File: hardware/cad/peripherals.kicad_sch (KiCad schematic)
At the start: 31 parts, among them J12 6-440054-2, J13 6-440054-2, J14 6-440129-2, J15 6-440129-2, J17 6-440054-2, J18 6-440054-2, J19 6-440129-2, J20 6-440129-2, Q1 DMN63D8LDW, SW1 FOOTSWITCH, SW2 FOOTSWITCH, U2 74LVC2G17

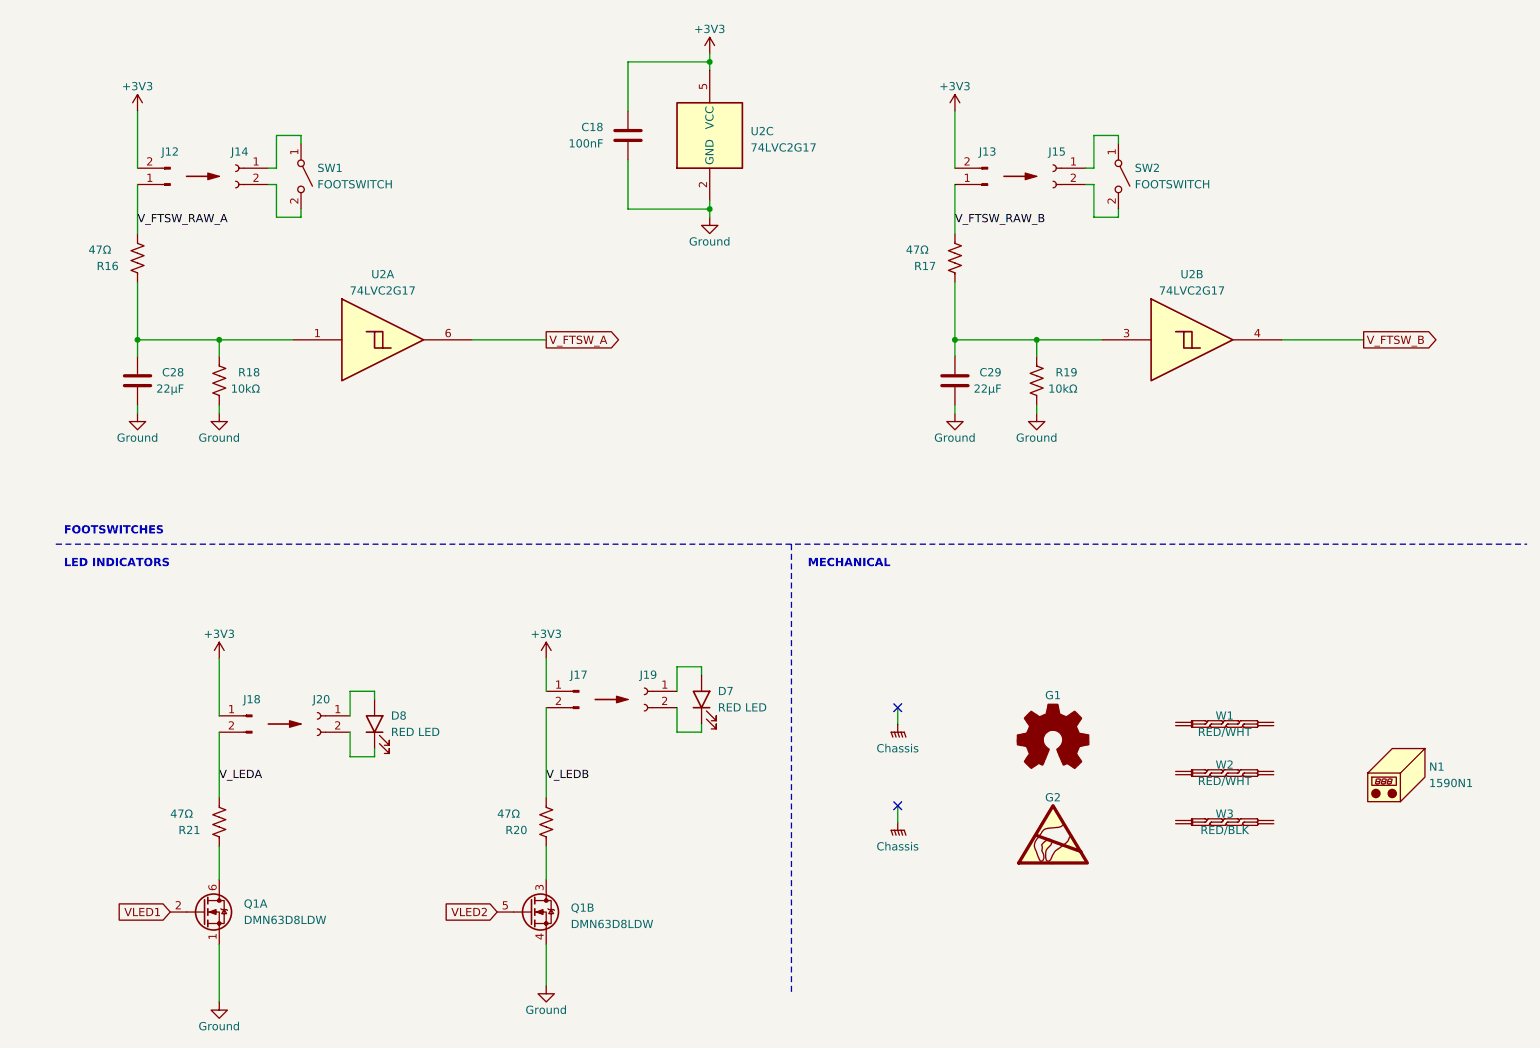
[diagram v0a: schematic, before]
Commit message: added differential inputs and started new layout
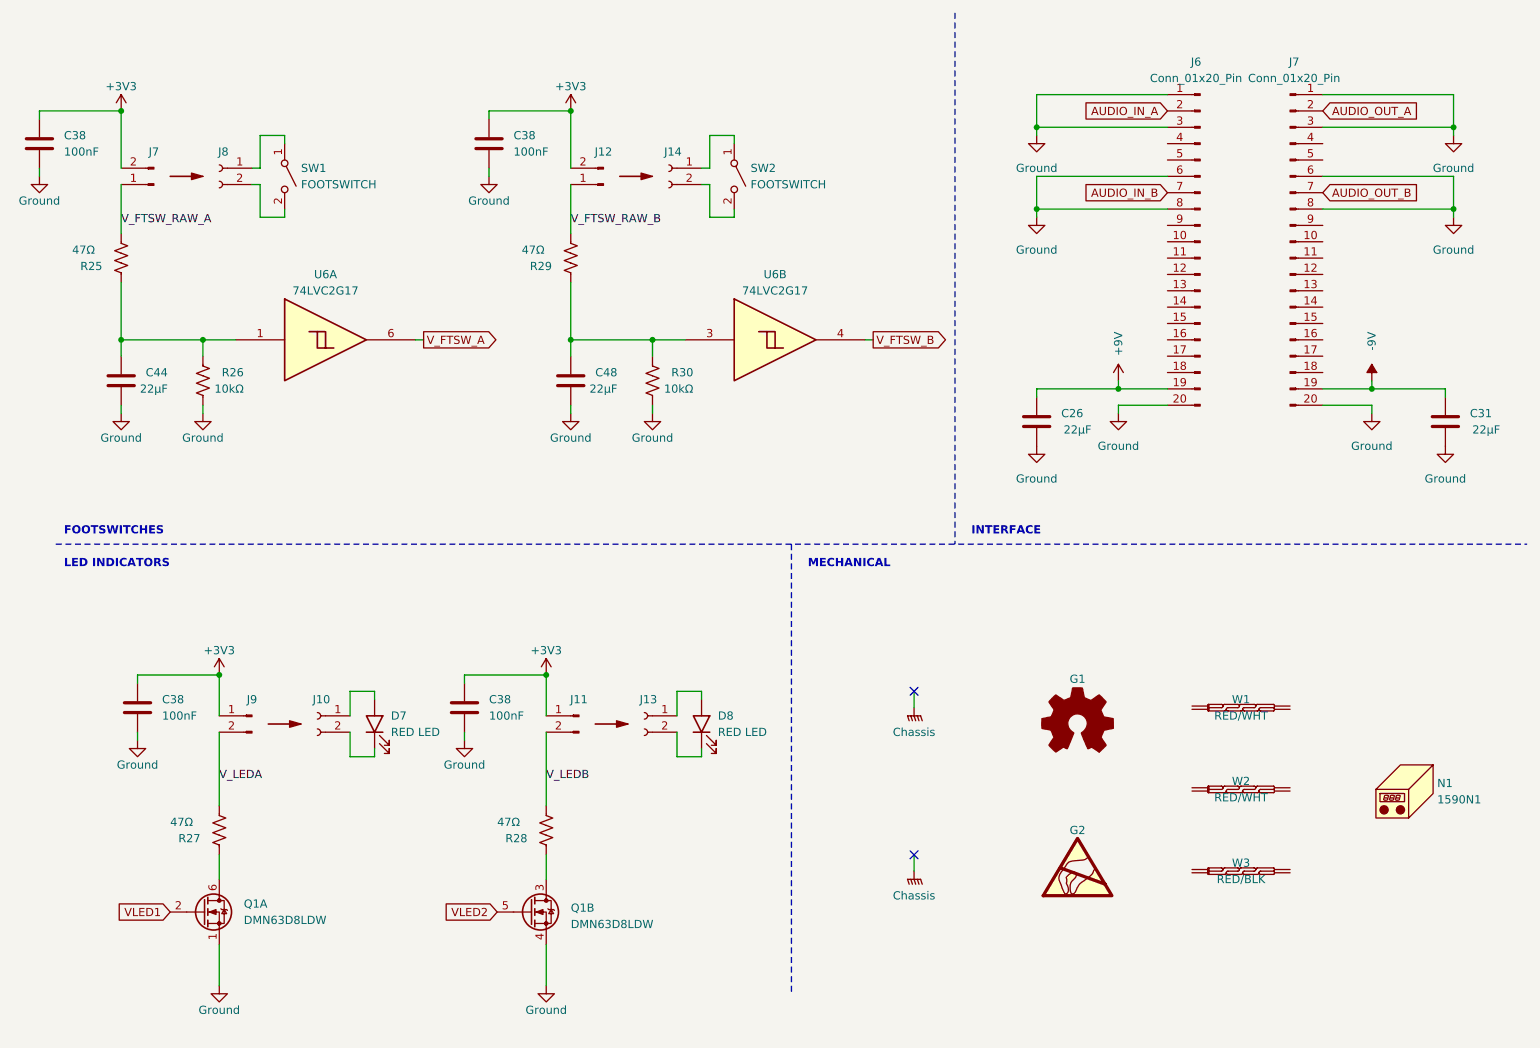
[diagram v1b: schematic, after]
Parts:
- removed C18: 100nF, Capacitor_SMD:C_0805_2012Metric, symbol Device:C
- removed unit 3 of U2
- added C26, C31: 22μF, Capacitor_SMD:C_0805_2012Metric, symbol Device:C
- added C38 (x4): 100nF, Capacitor_SMD:C_0805_2012Metric, symbol Device:C
- added J6, J7: Conn_01x20_Pin, Connector_PinSocket_2.54mm:PinSocket_1x20_P2.54mm_Vertical, symbol Connector:Conn_01x20_Pin
- renumbered C28 to C44, C29 to C48, D8 to D7, D7 to D8, J20 to J10, J17 to J11, J13 to J12, J19 to J13, J15 to J14, J12 to J7, J14 to J8, J18 to J9, R16 to R25, R18 to R26, R21 to R27, R20 to R28, R17 to R29, R19 to R30, U2 to U6
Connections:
- net +3V3: now also C38.2, C38.2, C38.2, C38.2
- net GND: now also C26.1, C31.1, C38.1, C38.1, C38.1, C38.1, J6.1 (Pin_1), J6.20 (Pin_20), J6.3 (Pin_3), J6.6 (Pin_6), J6.8 (Pin_8), J7.1 (Pin_1), J7.20 (Pin_20), J7.3 (Pin_3), J7.6 (Pin_6), J7.8 (Pin_8)
- new net +9V: C26.2, J6.19 (Pin_19)
- new net -9V: C31.2, J7.19 (Pin_19)
- new net AUDIO_IN_A: J6.2 (Pin_2)
- new net AUDIO_IN_B: J6.7 (Pin_7)
- new net AUDIO_OUT_A: J7.2 (Pin_2)
- new net AUDIO_OUT_B: J7.7 (Pin_7)
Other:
- note added: "INTERFACE"
- moved on the sheet: C44, C48, D8, G1, G2, J11, J12, J13, J14, J7, J8, N1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

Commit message: more layout updates
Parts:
- C26, C31: value 22μF -> 22u
- C38: value 100nF -> 100n
- C41: renamed from C44; value 22μF -> 22u
- C45: renamed from C48; value 22μF -> 22u
- R25, R27, R28, R29: value 47Ω -> 47R
- R26, R30: value 10kΩ -> 10k
- renumbered G1 to G2, G2 to G3
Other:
- moved on the sheet: C26, C31, C38, D7, D8, J10, J11, J13, J6, J7, J9
